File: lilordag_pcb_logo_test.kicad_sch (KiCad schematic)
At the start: 4 parts

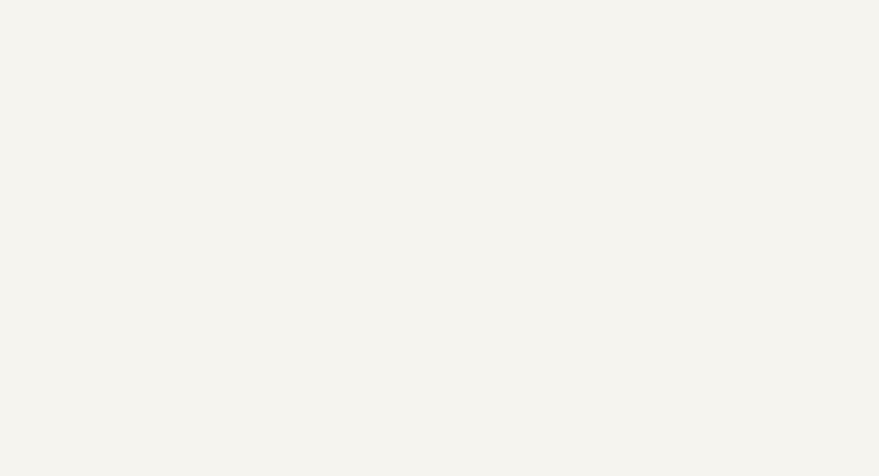
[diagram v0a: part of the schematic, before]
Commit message: Added astable multivibrator to the schematic.
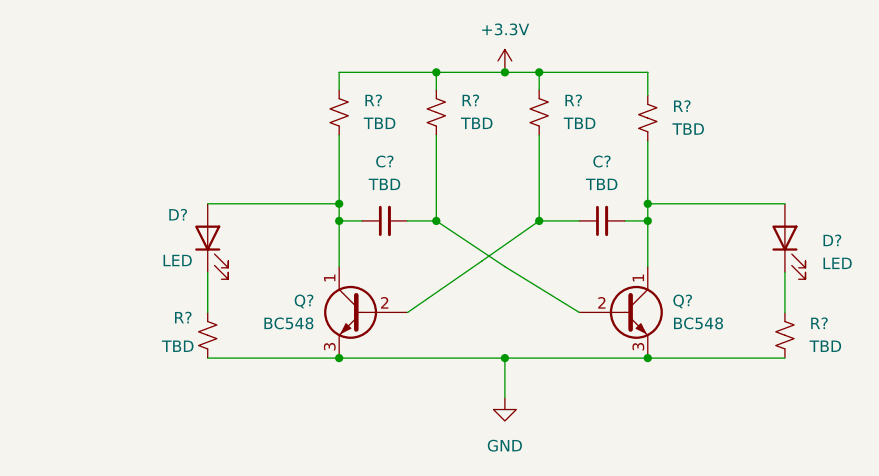
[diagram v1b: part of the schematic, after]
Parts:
- added C? (x2): TBD, symbol Device:C_Small
- added D? (x2): LED, symbol Device:LED
- added Q? (x2): BC548, Package_TO_SOT_THT:TO-92_Inline, symbol Transistor_BJT:BC548
- added R? (x6): TBD, symbol Device:R_Small_US
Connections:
- new net: C?.2, D?.2 (A), Q?.1 (C), R?.2
- new net: C?.2, Q?.2 (B), R?.2
- new net: D?.1 (K), R?.1 (x2)
- new net: C?.1, D?.2 (A), Q?.1 (C), R?.2
- new net: C?.1, Q?.2 (B), R?.2
- new net +3.3V: R?.1, R?.1, R?.1, R?.1
- new net GND: Q?.3 (E), Q?.3 (E), R?.2, R?.2

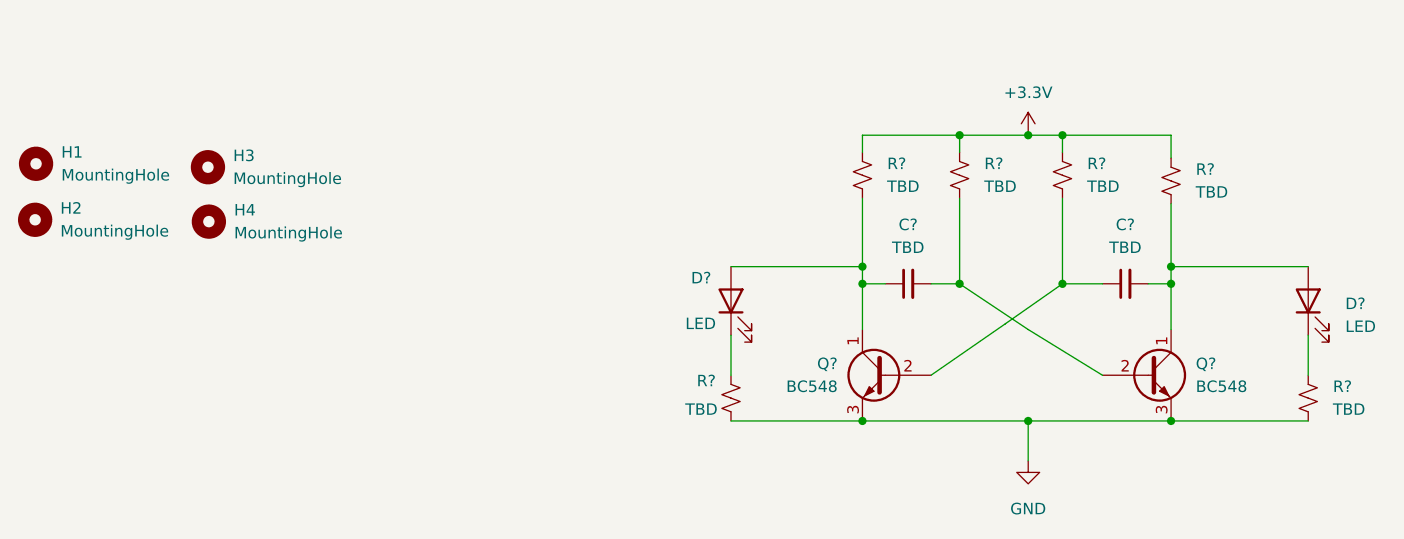
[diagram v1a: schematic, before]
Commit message: Added values to the astable multivibrator.
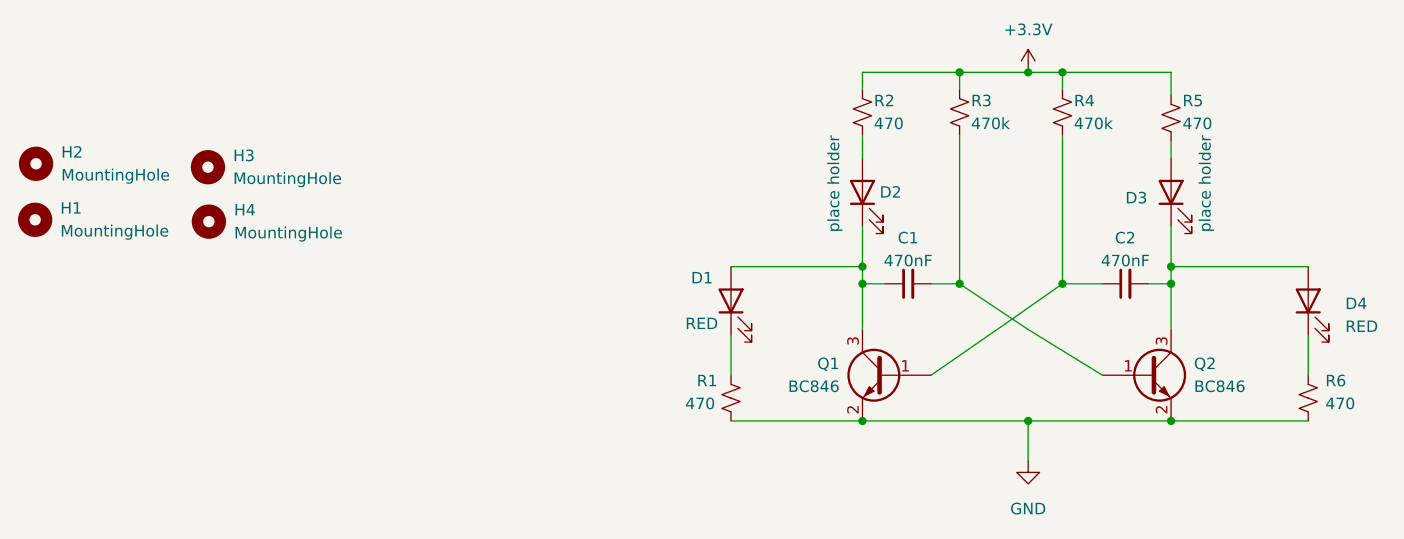
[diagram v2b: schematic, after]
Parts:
- removed Q? (x2): BC548, Package_TO_SOT_THT:TO-92_Inline, symbol Transistor_BJT:BC548
- added D2, D3: place holder, LED_SMD:LED_0603_1608Metric_Pad1.05x0.95mm_HandSolder, symbol Device:LED
- added Q1, Q2: BC846, Package_TO_SOT_SMD:SOT-23, symbol Transistor_BJT:BC846
- C1, C2: renamed from C?; value TBD -> 470nF; footprint (none) -> Capacitor_SMD:C_0603_1608Metric_Pad1.08x0.95mm_HandSolder
- D1, D4: renamed from D?; value LED -> RED; footprint (none) -> LED_SMD:LED_0603_1608Metric_Pad1.05x0.95mm_HandSolder
- R1, R2, R5, R6: renamed from R?; value TBD -> 470; footprint (none) -> Resistor_SMD:R_0603_1608Metric_Pad0.98x0.95mm_HandSolder
- R3, R4: renamed from R?; value TBD -> 470k; footprint (none) -> Resistor_SMD:R_0603_1608Metric_Pad0.98x0.95mm_HandSolder
- renumbered H2 to H1, H1 to H2
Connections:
- net GND: now also Q1.2 (E), Q2.2 (E)
- net at C2.2, D4.2 (A): now also D3.1 (K), Q2.3 (C); no longer R5.2
- net at C1.2, R3.2: now also Q2.1 (B)
- net at C1.1, D1.2 (A): now also D2.1 (K), Q1.3 (C); no longer R2.2
- net at C2.1, R4.2: now also Q1.1 (B)
- new net: D2.2 (A), R2.2
- new net: D3.2 (A), R5.2
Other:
- moved on the sheet: R2, R3, R4, R5

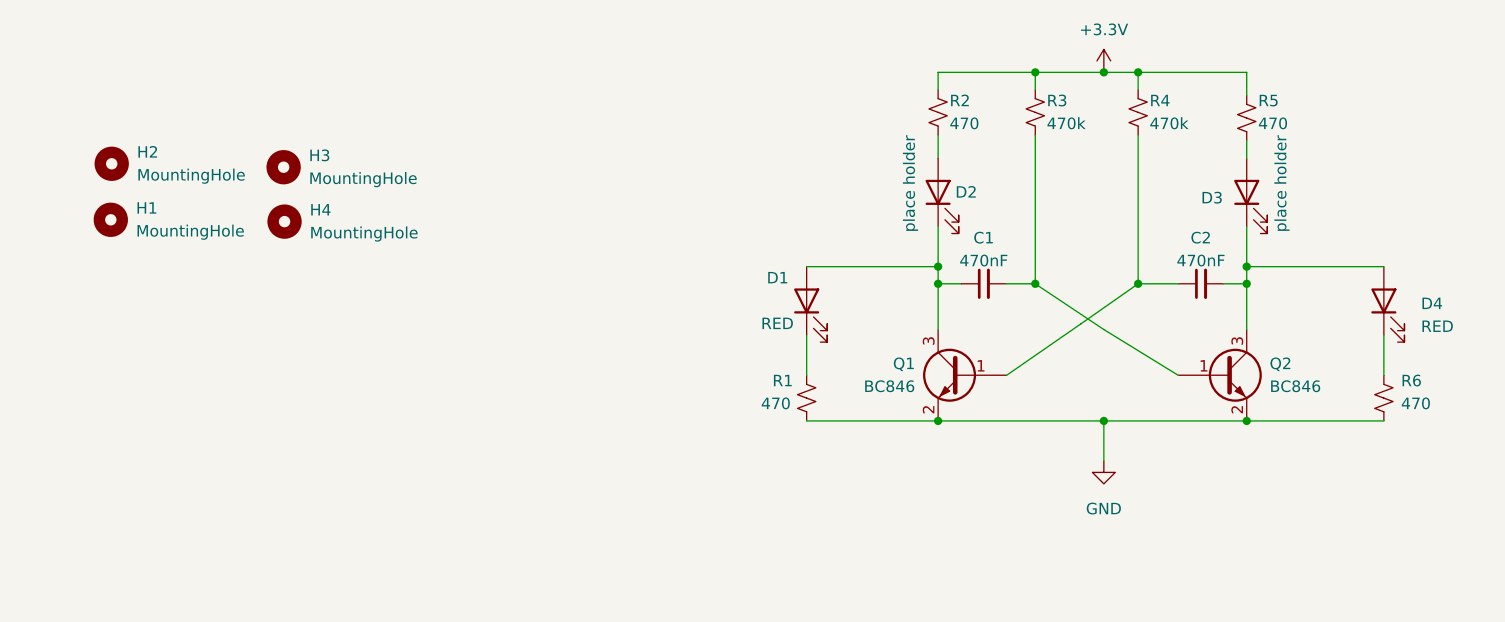
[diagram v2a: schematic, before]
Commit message: Added labels to the schematic.
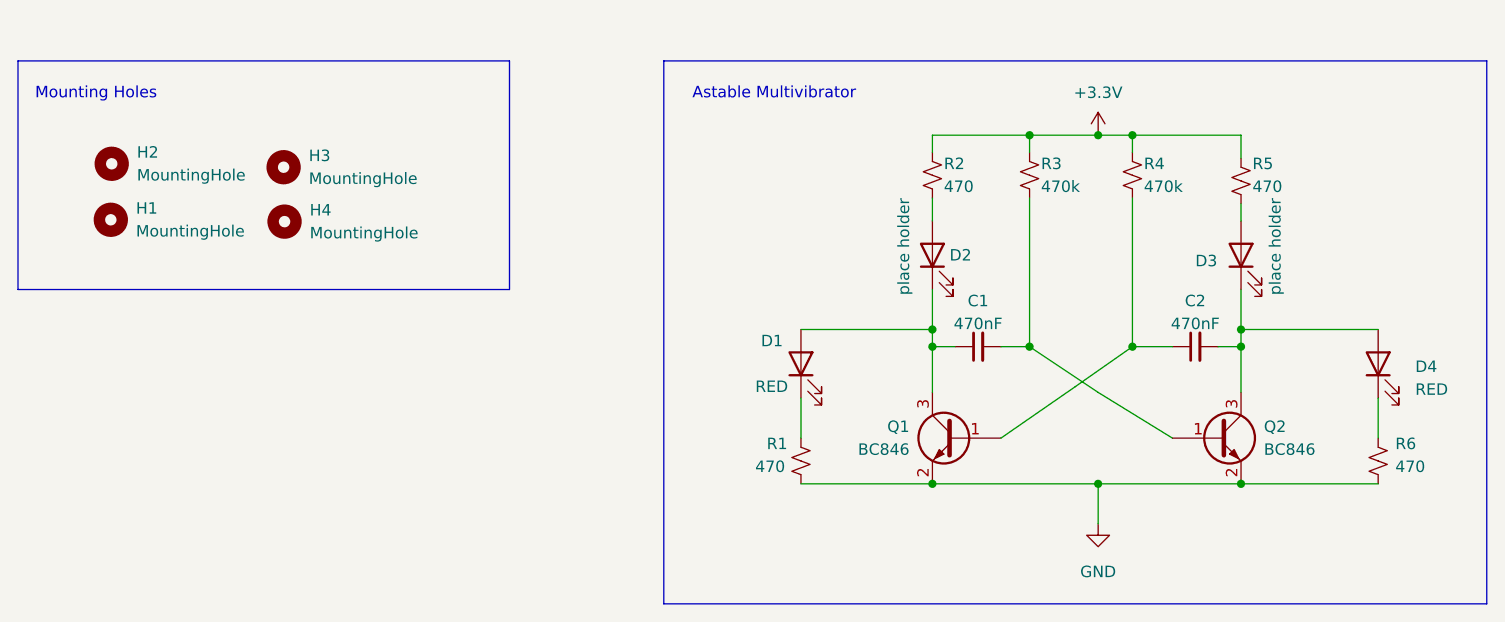
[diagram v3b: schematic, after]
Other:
- note added: "Astable Multivibrator"
- note added: "Mounting Holes"
- moved on the sheet: C1, C2, D1, D2, D3, D4, Q1, Q2, R1, R2, R3, R4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

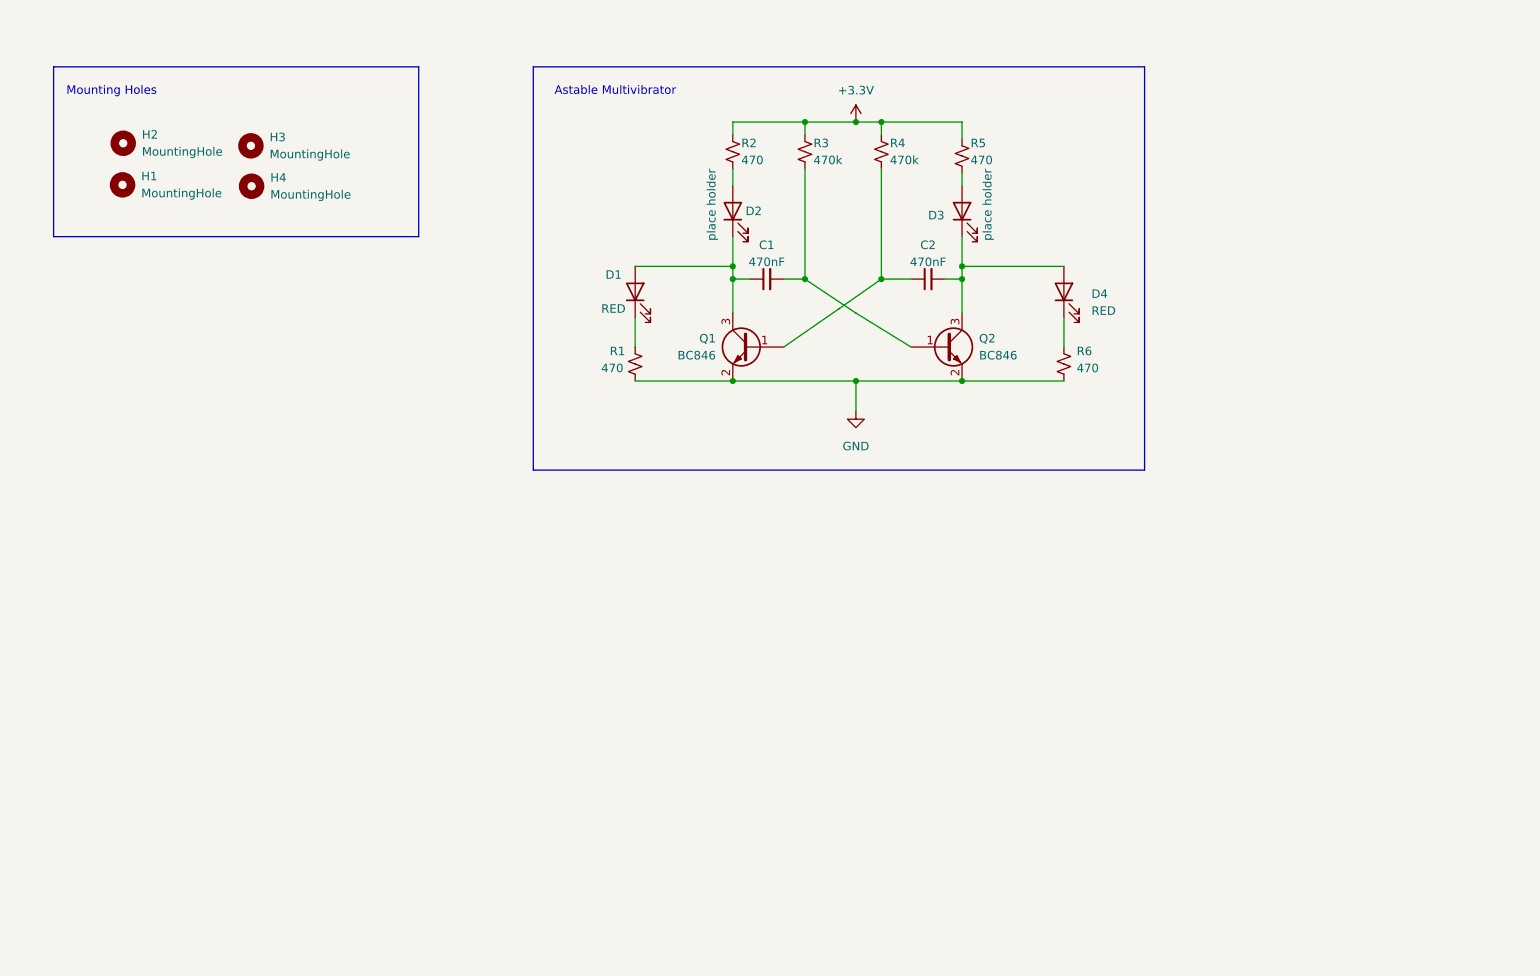
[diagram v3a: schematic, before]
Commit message: Added more LED's to tests loading multivibrator.
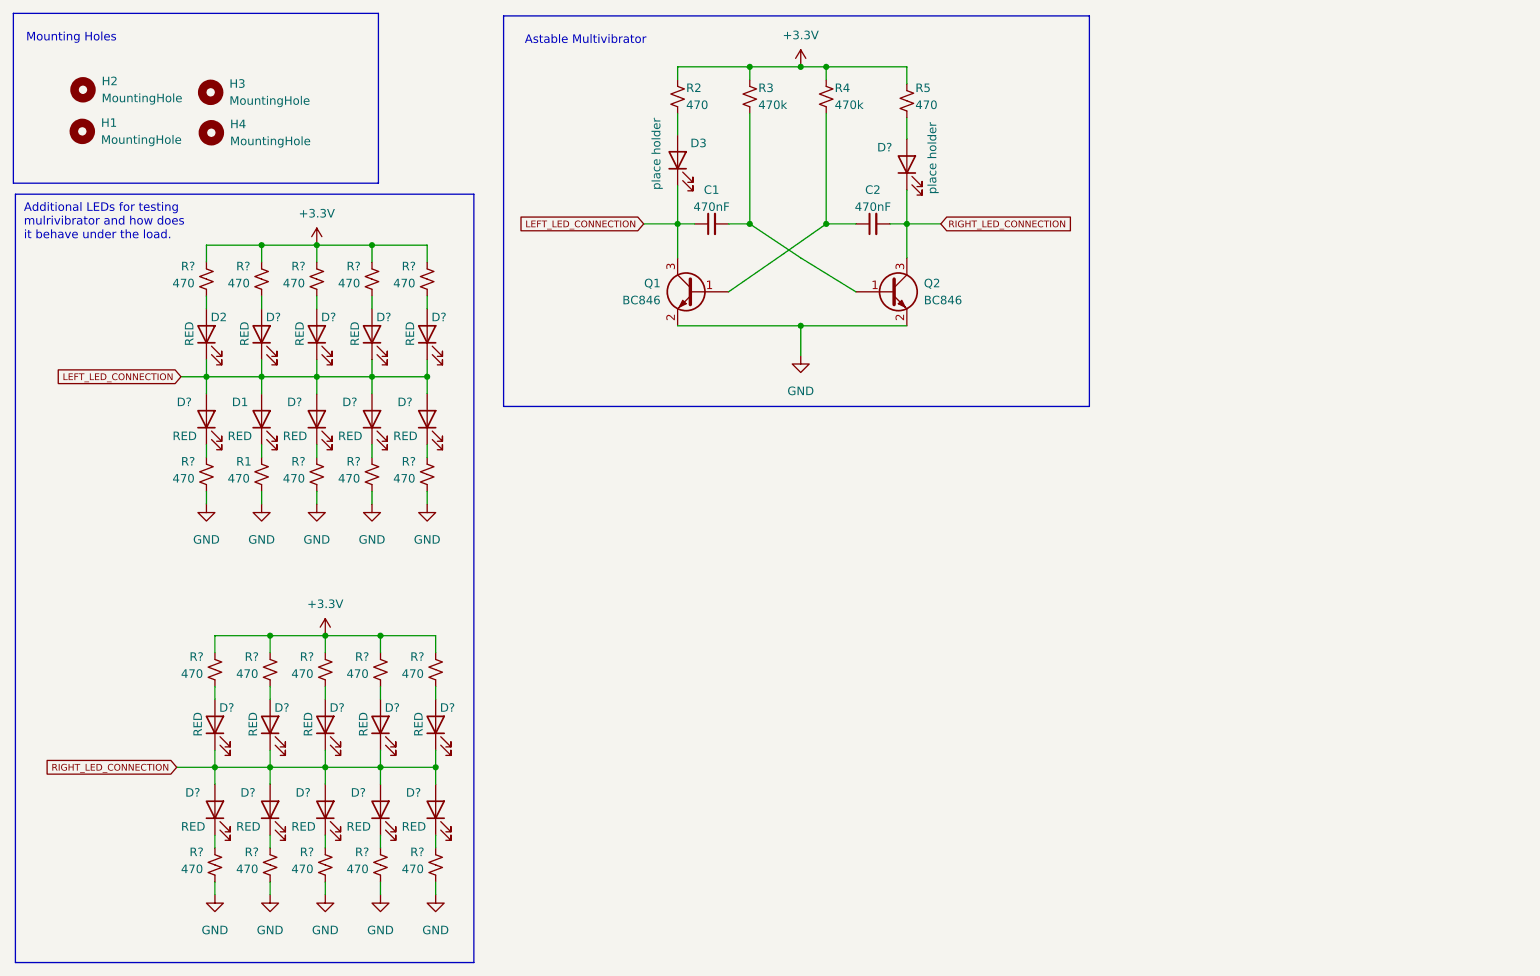
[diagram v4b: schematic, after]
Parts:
- removed D4: RED, LED_SMD:LED_0603_1608Metric_Pad1.05x0.95mm_HandSolder, symbol Device:LED
- removed R6: 470, Resistor_SMD:R_0603_1608Metric_Pad0.98x0.95mm_HandSolder, symbol Device:R_Small_US
- added D? (x18): RED, LED_SMD:LED_0603_1608Metric_Pad1.05x0.95mm_HandSolder, symbol Device:LED
- added D?: place holder, LED_SMD:LED_0603_1608Metric_Pad1.05x0.95mm_HandSolder, symbol Device:LED
- added R? (x19): 470, Resistor_SMD:R_0603_1608Metric_Pad0.98x0.95mm_HandSolder, symbol Device:R_Small_US
- D2: value place holder -> RED
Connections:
- net +3.3V: now also R?.1, R?.1, R?.1, R?.1, R?.1, R?.1, R?.1, R?.1, R?.1, R?.1
- net GND: now also R?.2, R?.2, R?.2, R?.2, R?.2, R?.2, R?.2, R?.2, R?.2
- net LEFT_LED_CONNECTION: now reaches C1.1, D1.2 (A), D2.1 (K), Q1.3 (C)
- net LEFT_LED_CONNECTION: now also D3.1 (K), D?.1 (K), D?.1 (K), D?.1 (K), D?.1 (K), D?.2 (A), D?.2 (A), D?.2 (A), D?.2 (A)
- net RIGHT_LED_CONNECTION: now reaches C2.2, Q2.3 (C)
- net RIGHT_LED_CONNECTION: now also D?.1 (K), D?.1 (K), D?.1 (K), D?.1 (K), D?.1 (K), D?.1 (K), D?.2 (A), D?.2 (A), D?.2 (A), D?.2 (A), D?.2 (A); no longer D3.1 (K)
- net at D2.2 (A): now also R?.2; no longer R2.2
- net at R5.2: now also D?.2 (A); no longer D3.2 (A)
- new net: D?.2 (A), R?.2 (x9)
- new net: D?.1 (K), R?.1 (x9)
- new net: D3.2 (A), R2.2
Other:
- note added: "Additional LEDs for testing mulrivibrator and how does it behave under the load."
- moved on the sheet: C1, C2, D1, D2, D3, H1, H2, H3, H4, Q1, Q2, R1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

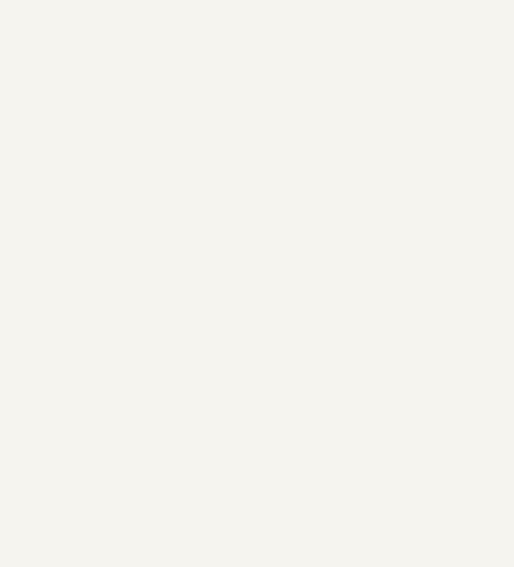
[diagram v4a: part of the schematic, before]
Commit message: Added the switch to the schematic.
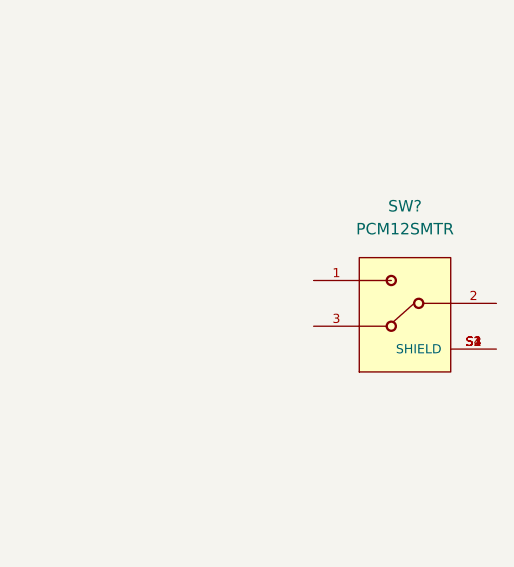
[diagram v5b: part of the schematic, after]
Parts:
- added SW?: PCM12SMTR, PCM12SMTR:SW_PCM12SMTR, symbol PCM12SMTR:PCM12SMTR
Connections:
- new net: SW?.S1 (SHIELD), SW?.S2 (SHIELD), SW?.S3 (SHIELD), SW?.S4 (SHIELD)
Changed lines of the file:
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@@
     )
+  )
+  (symbol (lib_id "PCM12SMTR:PCM12SMTR") (at 229.235 48.895 0) (unit 1)
+    (in_bom yes) (on_board yes) (fields_autoplaced)
+    (property "Reference" "SW?" (id 0) (at 229.235 38.1 0))
+    (property "Value" "PCM12SMTR" (id 1) (at 229.235 40.64 0))
+    (property "Footprint" "PCM12SMTR:SW_PCM12SMTR" (id 2) (at 229.235 48.895 0)
+      (effects (font (size 1.27 1.27)) (justify left bottom) hide)
+    )
+    (property "Datasheet" "" (id 3) (at 229.235 48.895 0)
+      (effects (font (size 1.27 1.27)) (justify left bottom) hide)
+    )
+    (property "MANUFACTURER" "C&K" (id 4) (at 229.235 48.895 0)
+      (effects (font (size 1.27 1.27)) (justify left bottom) hide)
+    )
+    (property "STANDARD" "Manufacturer Recommendation" (id 5) (at 229.235 48.895 0)
+      (effects (font (size 1.27 1.27)) (justify left bottom) hide)
+    )
+    (pin "1")
+    (pin "2")
+    (pin "3")
+    (pin "S1")
+    (pin "S2")
+    (pin "S3")
+    (pin "S4")
   )
   (symbol (lib_id "Device:R_Small_US") (at 66.675 81.915 0) (unit 1)
@@
       (reference "R?") (unit 1) (value "470") (footprint "Resistor_SMD:R_0603_1608Metric_Pad0.98x0.95mm_HandSolder")
     )
-  )
+    (path "/687250e6-d18c-45c2-bd11-81e20a77f3b0"
+      (reference "SW?") (unit 1) (value "PCM12SMTR") (footprint "PCM12SMTR:SW_PCM12SMTR")
+    )
+  )
